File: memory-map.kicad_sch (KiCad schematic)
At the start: 12 parts, among them K1 CONN_3, P2 CONN_4X2, U1 74LS04, U2 74LS244, U3 74LS682, U4 74LS86, U5 74LS02, U6 74LS00, U7 74LS32, U8 SRAM_512K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

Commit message: Schematic in progress
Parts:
- removed R1: 22K, R3, symbol Device:R
- K1: footprint PIN_ARRAY_3X1 -> Connector_PinHeader_2.54mm:PinHeader_1x03_P2.54mm_Vertical
- P1: renamed from P2; footprint PIN_ARRAY_4x2 -> Connector_PinHeader_2.54mm:PinHeader_2x04_P2.54mm_Vertical
- U1, U4, U5, U6, U7: footprint DIP-14__300 -> Package_DIP:DIP-14_W7.62mm_Socket_LongPads
- U2, U3: footprint DIP-20__300 -> Package_DIP:DIP-20_W7.62mm_Socket_LongPads
- U8: footprint Package_DIP:DIP-32_W15.24mm -> Package_DIP:DIP-32_W15.24mm_Socket_LongPads
- U9: footprint DIP-32__600 -> Package_DIP:DIP-32_W15.24mm_Socket_LongPads
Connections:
- net PULLUP2: now reaches K1.2 (Pin_2), U9.31 (PGM)
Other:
- note removed: "Can we find a 10K to 47K resistor pack to use here?"
- company: N8VEM Users Group -> (none)
- title: 6809 and 6502 ATX and 6U -> 6809PC

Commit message: PCB in progress
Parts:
- K1: value CONN_3 -> EPROM/FLASH; footprint Connector_PinHeader_2.54mm:PinHeader_1x03_P2.54mm_Vertical -> Custom:STD_DDW_PINHEAD_V_1x03
- P1: value CONN_4X2 -> SHADOW ADDR; footprint Connector_PinHeader_2.54mm:PinHeader_2x04_P2.54mm_Vertical -> Custom:STD_DDW_PINHEAD_V_2x04
- U1, U4, U5, U6, U7: footprint Package_DIP:DIP-14_W7.62mm_Socket_LongPads -> Custom:STD_DDW_DIP14
- U2, U3: footprint Package_DIP:DIP-20_W7.62mm_Socket_LongPads -> Custom:STD_DDW_DIP20
- U8, U9: footprint Package_DIP:DIP-32_W15.24mm_Socket_LongPads -> Custom:STD_DDW_DIP32
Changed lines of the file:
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@@
 			)
 		)
-		(property "Footprint" "Package_DIP:DIP-20_W7.62mm_Socket_LongPads"
+		(property "Footprint" "Custom:STD_DDW_DIP20"
 			(at 107.95 146.05 0)
 			(effects
@@
 		(on_board yes)
 		(dnp no)
-		(property "Reference" "#PWR09"
+		(property "Reference" "#PWR041"
 			(at 40.64 209.55 0)
 			(effects
@@
 			(project "6x0x-6U"
 				(path "/d94f9d60-5ece-4752-b49c-b0d1c95f35bc/00000000-0000-0000-0000-0000526c8ed2"
-					(reference "#PWR09")
+					(reference "#PWR041")
 					(unit 1)
 				)
@@
 			)
 		)
-		(property "Footprint" "Package_DIP:DIP-14_W7.62mm_Socket_LongPads"
+		(property "Footprint" "Custom:STD_DDW_DIP14"
 			(at 92.71 91.44 0)
 			(effects
@@
 			)
 		)
-		(property "Footprint" "Package_DIP:DIP-14_W7.62mm_Socket_LongPads"
+		(property "Footprint" "Custom:STD_DDW_DIP14"
 			(at 147.32 93.98 0)
 			(effects
@@
 			)
 		)
-		(property "Footprint" "Package_DIP:DIP-14_W7.62mm_Socket_LongPads"
+		(property "Footprint" "Custom:STD_DDW_DIP14"
 			(at 147.32 81.28 0)
 			(effects
@@
 			)
 		)
-		(property "Footprint" "Package_DIP:DIP-20_W7.62mm_Socket_LongPads"
+		(property "Footprint" "Custom:STD_DDW_DIP20"
 			(at 99.06 217.17 0)
 			(effects
@@
 			)
 		)
-		(property "Footprint" "Package_DIP:DIP-14_W7.62mm_Socket_LongPads"
+		(property "Footprint" "Custom:STD_DDW_DIP14"
 			(at 229.87 96.52 0)
 			(effects
@@
 			)
 		)
-		(property "Footprint" "Package_DIP:DIP-14_W7.62mm_Socket_LongPads"
+		(property "Footprint" "Custom:STD_DDW_DIP14"
 			(at 120.65 40.64 0)
 			(effects
@@
 			)
 		)
-		(property "Footprint" "Package_DIP:DIP-14_W7.62mm_Socket_LongPads"
+		(property "Footprint" "Custom:STD_DDW_DIP14"
 			(at 266.7 99.06 0)
 			(effects
@@
 			)
 		)
-		(property "Footprint" "Package_DIP:DIP-14_W7.62mm_Socket_LongPads"
+		(property "Footprint" "Custom:STD_DDW_DIP14"
 			(at 217.17 134.62 0)
 			(effects
@@
 			)
 		)
-		(property "Footprint" "Package_DIP:DIP-14_W7.62mm_Socket_LongPads"
+		(property "Footprint" "Custom:STD_DDW_DIP14"
 			(at 262.89 132.08 0)
 			(effects
@@
 			)
 		)
-		(property "Footprint" "Package_DIP:DIP-32_W15.24mm_Socket_LongPads"
+		(property "Footprint" "Custom:STD_DDW_DIP32"
 			(at 355.6 68.58 0)
 			(effects
@@
 			)
 		)
-		(property "Footprint" "Package_DIP:DIP-32_W15.24mm_Socket_LongPads"
+		(property "Footprint" "Custom:STD_DDW_DIP32"
 			(at 350.52 160.02 0)
 			(effects
@@
 			)
 		)
-		(property "Footprint" "Package_DIP:DIP-14_W7.62mm_Socket_LongPads"
+		(property "Footprint" "Custom:STD_DDW_DIP14"
 			(at 147.32 58.42 0)
 			(effects
@@
 			)
 		)
-		(property "Footprint" "Package_DIP:DIP-14_W7.62mm_Socket_LongPads"
+		(property "Footprint" "Custom:STD_DDW_DIP14"
 			(at 147.32 43.18 0)
 			(effects
@@
 			)
 		)
-		(property "Value" "CONN_4X2"
+		(property "Value" "SHADOW ADDR"
 			(at 46.99 162.306 90)
 			(effects
@@
 			)
 		)
-		(property "Footprint" "Connector_PinHeader_2.54mm:PinHeader_2x04_P2.54mm_Vertical"
+		(property "Footprint" "Custom:STD_DDW_PINHEAD_V_2x04"
 			(at 45.72 161.29 0)
 			(effects
@@
 		(on_board yes)
 		(dnp no)
-		(property "Reference" "#PWR010"
+		(property "Reference" "#PWR042"
 			(at 43.18 179.07 0)
 			(effects
@@
 			(project "6x0x-6U"
 				(path "/d94f9d60-5ece-4752-b49c-b0d1c95f35bc/00000000-0000-0000-0000-0000526c8ed2"
-					(reference "#PWR010")
+					(reference "#PWR042")
 					(unit 1)
 				)
@@
 			)
 		)
-		(property "Value" "CONN_3"
+		(property "Value" "EPROM/FLASH"
 			(at 317.5 120.65 90)
 			(effects
@@
 			)
 		)
-		(property "Footprint" "Connector_PinHeader_2.54mm:PinHeader_1x03_P2.54mm_Vertical"
+		(property "Footprint" "Custom:STD_DDW_PINHEAD_V_1x03"
 			(at 317.5 118.11 0)
 			(effects
@@
 		(on_board yes)
 		(dnp no)
-		(property "Reference" "#PWR017"
+		(property "Reference" "#PWR049"
 			(at 355.6 36.83 0)
 			(effects
@@
 			(project "6x0x-6U"
 				(path "/d94f9d60-5ece-4752-b49c-b0d1c95f35bc/00000000-0000-0000-0000-0000526c8ed2"
-					(reference "#PWR017")
+					(reference "#PWR049")
 					(unit 1)
 				)
@@
 		(on_board yes)
 		(dnp no)
-		(property "Reference" "#PWR018"
+		(property "Reference" "#PWR050"
 			(at 355.6 118.11 0)
 			(effects
@@
 			(project "6809PC-6U"
 				(path "/d94f9d60-5ece-4752-b49c-b0d1c95f35bc/00000000-0000-0000-0000-0000526c8ed2"
-					(reference "#PWR018")
+					(reference "#PWR050")
 					(unit 1)
 				)
@@
 		(on_board yes)
 		(dnp no)
-		(property "Reference" "#PWR011"
+		(property "Reference" "#PWR043"
 			(at 99.06 194.31 0)
 			(effects
@@
 			(project "6809PC-6U"
 				(path "/d94f9d60-5ece-4752-b49c-b0d1c95f35bc/00000000-0000-0000-0000-0000526c8ed2"
-					(reference "#PWR011")
+					(reference "#PWR043")
 					(unit 1)
 				)
@@
 		(on_board yes)
 		(dnp no)
-		(property "Reference" "#PWR015"
+		(property "Reference" "#PWR047"
 			(at 350.52 130.81 0)
 			(effects
@@
 			(project "6809PC-6U"
 				(path "/d94f9d60-5ece-4752-b49c-b0d1c95f35bc/00000000-0000-0000-0000-0000526c8ed2"
-					(reference "#PWR015")
+					(reference "#PWR047")
 					(unit 1)
 				)
@@
 		(on_board yes)
 		(dnp no)
-		(property "Reference" "#PWR016"
+		(property "Reference" "#PWR048"
 			(at 350.52 193.04 0)
 			(effects
@@
 			(project "6809PC-6U"
 				(path "/d94f9d60-5ece-4752-b49c-b0d1c95f35bc/00000000-0000-0000-0000-0000526c8ed2"
-					(reference "#PWR016")
+					(reference "#PWR048")
 					(unit 1)
 				)
@@
 		(on_board yes)
 		(dnp no)
-		(property "Reference" "#PWR012"
+		(property "Reference" "#PWR044"
 			(at 99.06 237.49 0)
 			(effects
@@
 			(project "6809PC-6U"
 				(path "/d94f9d60-5ece-4752-b49c-b0d1c95f35bc/00000000-0000-0000-0000-0000526c8ed2"
-					(reference "#PWR012")
+					(reference "#PWR044")
 					(unit 1)
 				)
@@
 		(on_board yes)
 		(dnp no)
-		(property "Reference" "#PWR013"
+		(property "Reference" "#PWR045"
 			(at 107.95 95.25 0)
 			(effects
@@
 			(project "6809PC-6U"
 				(path "/d94f9d60-5ece-4752-b49c-b0d1c95f35bc/00000000-0000-0000-0000-0000526c8ed2"
-					(reference "#PWR013")
+					(reference "#PWR045")
 					(unit 1)
 				)
@@
 		(on_board yes)
 		(dnp no)
-		(property "Reference" "#PWR014"
+		(property "Reference" "#PWR046"
 			(at 107.95 194.31 0)
 			(effects
@@
 			(project "6809PC-6U"
 				(path "/d94f9d60-5ece-4752-b49c-b0d1c95f35bc/00000000-0000-0000-0000-0000526c8ed2"
-					(reference "#PWR014")
+					(reference "#PWR046")
 					(unit 1)
 				)

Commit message: 6809PC work
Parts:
- removed unit 2 of U4
- removed unit 4 of U5
- removed U9: 29F040, Custom:STD_DDW_DIP32, symbol Memory_Flash:SST39SF040
- added U9: 27C64, Package_DIP:DIP-28_W15.24mm, symbol Memory_EPROM:27C64
- K1: value EPROM/FLASH -> ROM SELECT
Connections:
- net /RD: now also U9.22 (~{OE})
- net /WR: no longer K1.1 (Pin_1)
- net GND: now also K1.1 (Pin_1), U9.14 (GND)
- net PULLUP2: now also U9.27 (~{PGM}); no longer K1.2 (Pin_2)
- net SHADOW-ROM: now also U7.1
- net VCC: now also U9.28 (VCC)
- net mA0: now also U9.10 (A0)
- net mA1: now also U9.9 (A1)
- net mA10: now also U9.21 (A10)
- net mA11: now also U9.23 (A11)
- net mA18: no longer K1.3 (Pin_3)
- net mA2: now also U9.8 (A2)
- net mA3: now also U9.7 (A3)
- net mA4: now also U9.6 (A4)
- net mA5: now also U9.5 (A5)
- net mA6: now also U9.4 (A6)
- net mA7: now also U9.3 (A7)
- net mA8: now also U9.25 (A8)
- net mA9: now also U9.24 (A9)
- net mD0: now also U9.11 (D0)
- net mD1: now also U9.12 (D1)
- net mD2: now also U9.13 (D2)
- net mD3: now also U9.15 (D3)
- net mD4: now also U9.16 (D4)
- net mD5: now also U9.17 (D5)
- net mD6: now also U9.18 (D6)
- net mD7: now also U9.19 (D7)
- net at U7.3: now also U9.20 (~{CE})
- new net: K1.2 (Pin_2), U9.2 (A12)
- new net PULLUP3: K1.3 (Pin_3)
- no-connect marks 1 -> 2
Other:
- note added: "HIGH"
- note added: "LOW"
- note removed: "*"
- note removed: "* for EPROM, A18 will satisfy the requirement of being equal to either Vih or Vil at all times."
- note removed: "EPROM"
- note removed: "FLASH"
- note removed: "mA19 != RAM-A19"

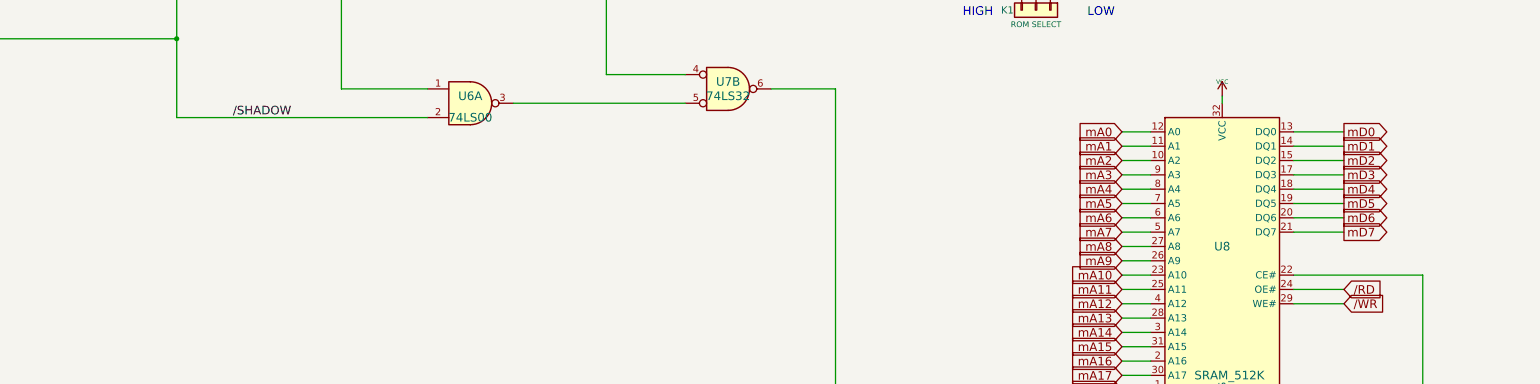
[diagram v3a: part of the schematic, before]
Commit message: fix issue with ISA RW select lines
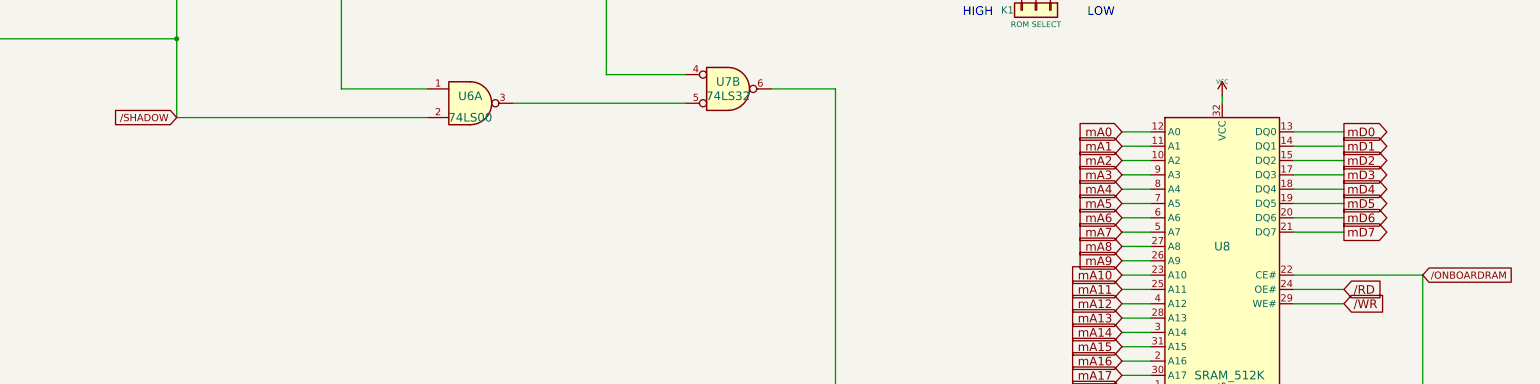
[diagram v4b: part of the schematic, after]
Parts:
- U9: footprint Package_DIP:DIP-28_W15.24mm -> Custom:STD_DDW_DIP28
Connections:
- net /ONBOARDRAM: now reaches U7.6, U8.22 (CE#)
- net /SHADOW renamed /SHADOW
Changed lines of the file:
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@@
 		)
 	)
-	(label "/SHADOW"
-		(at 185.42 137.16 180)
-		(fields_autoplaced yes)
-		(effects
-			(font
-				(size 1.524 1.524)
-			)
-			(justify right bottom)
-		)
-	)
 	(global_label "mD2"
 		(shape output)
@@
 		)
 	)
+	(global_label "{slash}SHADOW"
+		(shape input)
+		(at 165.1 137.16 180)
+		(fields_autoplaced yes)
+		(effects
+			(font
+				(size 1.27 1.27)
+			)
+			(justify right)
+		)
+		(property "Intersheetrefs" "${INTERSHEET_REFS}"
+			(at 153.758 137.16 0)
+			(effects
+				(font
+					(size 1.27 1.27)
+				)
+				(justify right)
+				(hide yes)
+			)
+		)
+	)
 	(global_label "mA16"
 		(shape input)
@@
 		)
 	)
+	(global_label "{slash}ONBOARDRAM"
+		(shape input)
+		(at 386.08 165.1 0)
+		(fields_autoplaced yes)
+		(effects
+			(font
+				(size 1.27 1.27)
+			)
+			(justify left)
+		)
+		(property "Intersheetrefs" "${INTERSHEET_REFS}"
+			(at 402.4416 165.1 0)
+			(effects
+				(font
+					(size 1.27 1.27)
+				)
+				(justify left)
+				(hide yes)
+			)
+		)
+	)
 	(global_label "mD7"
 		(shape output)
@@
 			)
 		)
-		(property "Footprint" "Package_DIP:DIP-28_W15.24mm"
+		(property "Footprint" "Custom:STD_DDW_DIP28"
 			(at 360.68 66.04 0)
 			(effects

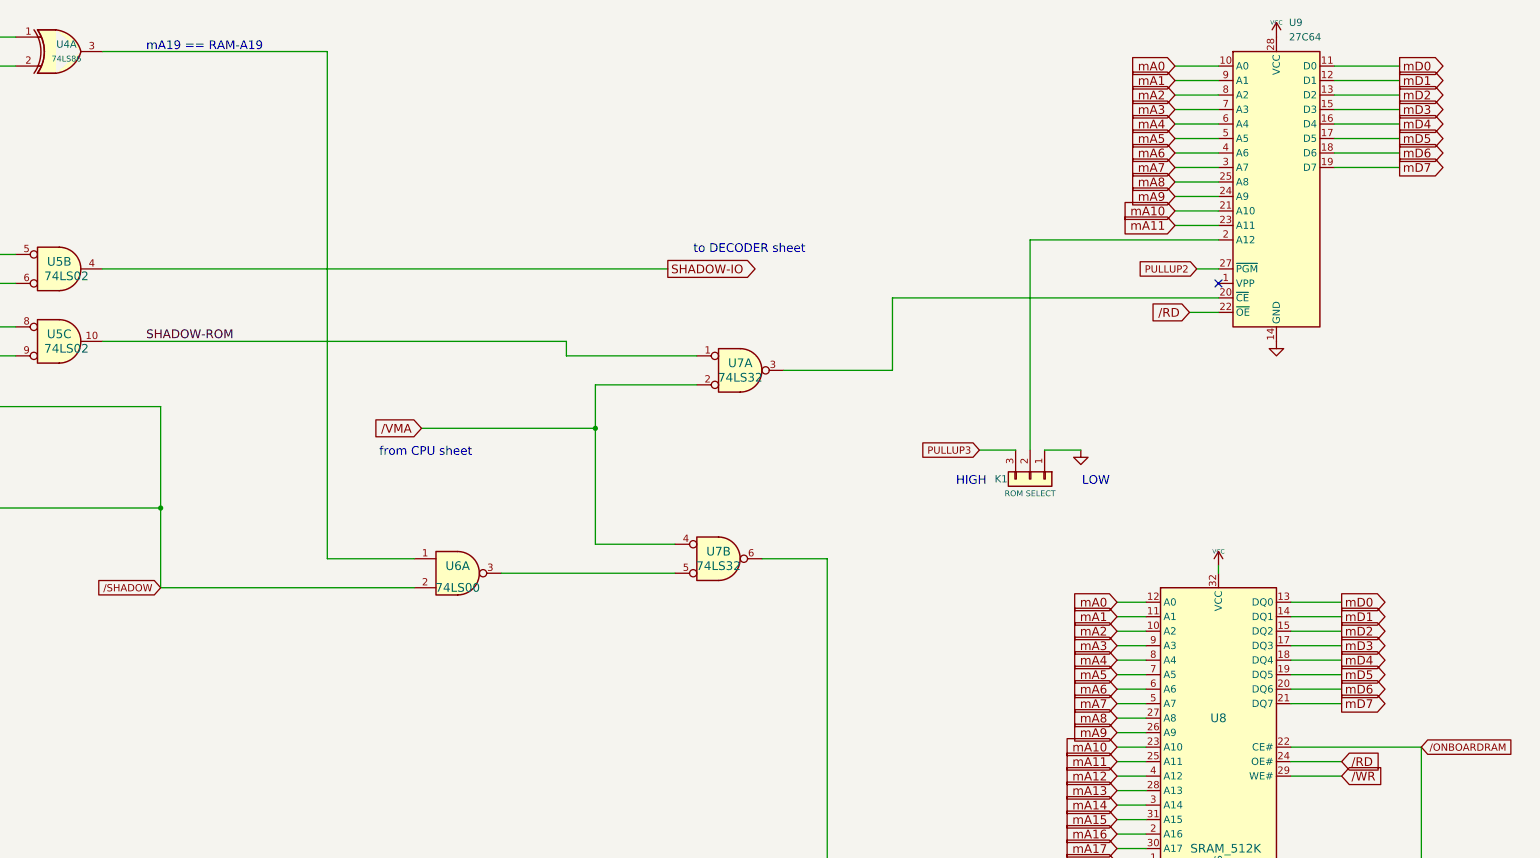
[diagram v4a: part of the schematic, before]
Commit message: fix bus issue
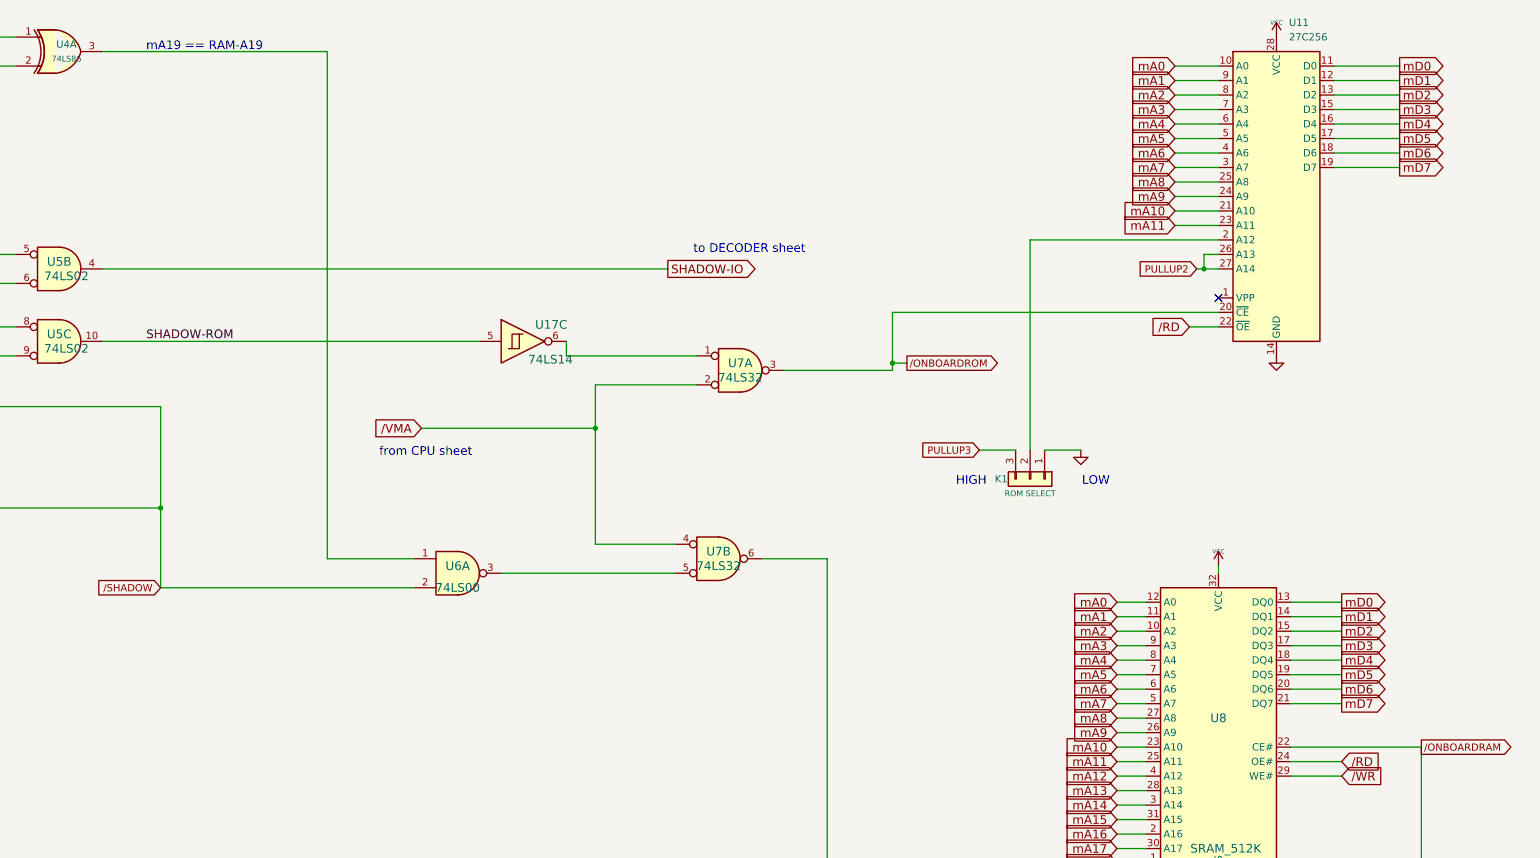
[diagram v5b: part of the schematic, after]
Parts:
- removed U9: 27C64, Custom:STD_DDW_DIP28, symbol Memory_EPROM:27C64
- added U11: 27C256, Package_DIP:DIP-28_W15.24mm, symbol Memory_EPROM:27C256
- added U17: 74LS14, Custom:STD_DDW_DIP14, symbol 74xx:74LS14
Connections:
- net /RD: now also U11.22 (~{OE})
- net GND: now also U11.14 (GND)
- net PULLUP2: now also U11.26 (A13), U11.27 (A14)
- net SHADOW-ROM: now also U17.5; no longer U7.1
- net VCC: now also U11.28 (VCC)
- net mA0: now also U11.10 (A0)
- net mA1: now also U11.9 (A1)
- net mA10: now also U11.21 (A10)
- net mA11: now also U11.23 (A11)
- net mA2: now also U11.8 (A2)
- net mA3: now also U11.7 (A3)
- net mA4: now also U11.6 (A4)
- net mA5: now also U11.5 (A5)
- net mA6: now also U11.4 (A6)
- net mA7: now also U11.3 (A7)
- net mA8: now also U11.25 (A8)
- net mA9: now also U11.24 (A9)
- net mD0: now also U11.11 (D0)
- net mD1: now also U11.12 (D1)
- net mD2: now also U11.13 (D2)
- net mD3: now also U11.15 (D3)
- net mD4: now also U11.16 (D4)
- net mD5: now also U11.17 (D5)
- net mD6: now also U11.18 (D6)
- net mD7: now also U11.19 (D7)
- net /ONBOARDROM: now reaches U7.3
- net /ONBOARDROM: now also U11.20 (~{CE})
- net at K1.2 (Pin_2): now also U11.2 (A12)
- new net: U17.6, U7.1
